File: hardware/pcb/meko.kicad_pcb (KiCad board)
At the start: 2 copper layers, 16 parts, among them IC1 MCP16502AD, IC2 MAYA-W386-00B, J1 Micro_SD_Card_Det1, J2 Micro_SD_Card_Det1, J4 Conn_ARM_JTAG_SWD_10, U1 SAMA7D65-4HB, U2 K4E8E324EB-EGCF, U3 MAX17260, U5 ECMF02-2AMX6, Y1 32kHz768, Y2 24MHz, Y3 32kHz768

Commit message: bunch of small audio changes
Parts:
- added IC3: TAC5212, Package_DFN_QFN:VQFN-24-1EP_4x4mm_P0.5mm_EP2.45x2.45mm, F.Cu at (100.9, 98.6)
- added J3: USB_C_Receptacle_USB2.0_16P, PCM_ckl-connector:USB_C_Receptacle_HRO_TYPE-C-31-M-12, F.Cu at (151.4, 55.9)
- added J5: 503480-1000, 503480-1000:5034801000, F.Cu at (95.8, 49.1)
- added J6: PJ-342, PCM_ckl-connector:Jack_3.5mm_SHOUHAN_PJ-342, F.Cu at (144.7, 39.9)
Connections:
- U1 pad P16: unconnected-(U1GPIO A&B-PA4-PadP16) -> /SAMA7/EXT.DAT1
- U1 pad R12: unconnected-(U1GPIO A&B-PA10-PadR12) -> /SAMA7/EXT.DAT3
- U1 pad T18: unconnected-(U1GPIO A&B-PA3-PadT18) -> /SAMA7/EXT.DAT0
- U1 pad U14: unconnected-(U1GPIO A&B-PA9-PadU14) -> /SAMA7/EXT.DAT2
- U1 pad U18: unconnected-(U1GPIO A&B-PA0-PadU18) -> /SAMA7/EXT.CK
- U1 pad V15: unconnected-(U1GPIO A&B-PA16-PadV15) -> /SAMA7/EXT.CD
- U1 pad V17: unconnected-(U1GPIO A&B-PA1-PadV17) -> /SAMA7/EXT.CMD

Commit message: bunch of small audio changes
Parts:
- added J7: PJ-342, PJ242:Jack_2.5mm_PJ242_6P_12x6.2x4mm_Horizontal, F.Cu at (148.6, 30.6)
- added U6: TPS7A2033PDBV, Package_TO_SOT_SMD:SOT-23-5, F.Cu at (152.0, 22.1)
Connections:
- IC3 pad 1: unconnected-(IC3-DREG-Pad1) -> Net-(IC3-DREG)
- IC3 pad 10: unconnected-(IC3-GPIO2-Pad10) -> /Audio/GPIO2
- IC3 pad 11: unconnected-(IC3-GPO1-Pad11) -> /Audio/GPO1
- IC3 pad 12: unconnected-(IC3-GPI1-Pad12) -> /Audio/GPI1
- IC3 pad 2: unconnected-(IC3-BCLK-Pad2) -> /Audio/BCLK
- IC3 pad 23: unconnected-(IC3-AVDD-Pad23) -> +3V3_AVDD
- IC3 pad 24: unconnected-(IC3-VREF-Pad24) -> Net-(IC3-VREF)
- IC3 pad 3: unconnected-(IC3-FSYNC-Pad3) -> /Audio/FSYNC
- IC3 pad 4: unconnected-(IC3-DOUT-Pad4) -> /Audio/DOUT
- IC3 pad 5: unconnected-(IC3-DIN-Pad5) -> /Audio/DIN
- IC3 pad 6: unconnected-(IC3-IOVDD-Pad6) -> +3V3
- IC3 pad 9: unconnected-(IC3-GPIO1-Pad9) -> /Audio/GPIO1
- J6 pad R1: (no net) -> unconnected-(J6-PadR1)
- J6 pad R1N: (no net) -> unconnected-(J6-PadR1N)
- J6 pad R2: (no net) -> unconnected-(J6-PadR2)
- J6 pad S: (no net) -> unconnected-(J6-PadS)
- J6 pad T: (no net) -> unconnected-(J6-PadT)
- J6 pad TN: (no net) -> unconnected-(J6-PadTN)

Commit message: moved stuff around
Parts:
- removed U2: K4E8E324EB-EGCF, K4E6E304EC-EGCG:FBGA-178_L11.5-W11.0_K4E6E304EC-TL
- added U7: DRV2605LDGS, Package_SO:TSSOP-10_3x3mm_P0.5mm, F.Cu at (157.5, 139.8)
- added U8: MT41K256M16TW, Package_BGA:Micron_FBGA-96_8x14mm_Layout9x16_P0.8mm, F.Cu at (105.3, 113.7)
- IC1: value MCP16502AD -> MCP16502AB
- J7: value PJ-342 -> PJ-242
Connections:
- net +1V2_DDR renamed +1V35_DDR
- IC1 pad 17: GND -> unconnected-(IC1-SELV2-Pad17)
- IC2 pad A2: unconnected-(IC2-1V8-PadA2) -> +1V8
- IC2 pad A3: unconnected-(IC2-SD_DAT[1]-PadA3) -> /Wireless/DAT1
- IC2 pad A4: unconnected-(IC2-SD_CLK-PadA4) -> /Wireless/CK
- IC2 pad A5: unconnected-(IC2-SD_DAT[3]-PadA5) -> /Wireless/DAT3
- IC2 pad A7: 3V3 -> +3V3
- IC2 pad B3: unconnected-(IC2-SD_DAT[0]-PadB3) -> /Wireless/DAT0
- IC2 pad B4: unconnected-(IC2-SD_CMD-PadB4) -> /Wireless/CMD
- IC2 pad B5: unconnected-(IC2-SD_DAT[2]-PadB5) -> /Wireless/DAT2
- IC2 pad B7: 3V3 -> +3V3
- IC2 pad D8: unconnected-(IC2-PCM_CLK-PadD8) -> /Wireless/BCLK
- IC2 pad E7: unconnected-(IC2-BT_HOST_WAKE-PadE7) -> /Wireless/BT.HOST_WAKE
- IC2 pad E8: unconnected-(IC2-PCM_MCLK-PadE8) -> /Wireless/MCLK
- IC2 pad E9: unconnected-(IC2-PCM_DIN-PadE9) -> /Wireless/DIN
- IC2 pad F7: unconnected-(IC2-WL_HOST_WAKE-PadF7) -> /Wireless/WL.HOST_WAKE
- IC2 pad F8: unconnected-(IC2-PCM_SYNC-PadF8) -> /Wireless/FSYNC
- IC2 pad F9: unconnected-(IC2-PCM_DOUT-PadF9) -> /Wireless/DOUT
- IC2 pad G8: unconnected-(IC2-UART_RX-PadG8) -> /Wireless/RX
- IC2 pad G9: unconnected-(IC2-UART_TX-PadG9) -> /Wireless/TX
- IC2 pad H7: unconnected-(IC2-JTAG_SEL-PadH7) -> GND
- IC2 pad H8: unconnected-(IC2-UART_CTSN-PadH8) -> /Wireless/CTSN
- IC2 pad H9: unconnected-(IC2-UART_RTSN-PadH9) -> /Wireless/RTSN
- IC2 pad J3: unconnected-(IC2-WL_EN-PadJ3) -> /Wireless/WL.EN
- IC2 pad J7: unconnected-(IC2-BT_EN-PadJ7) -> /Wireless/BT.EN
- IC2 pad J8: unconnected-(IC2-WL_DEV_WAKE-PadJ8) -> /Wireless/WL.DEV_WAKE
- IC2 pad J9: unconnected-(IC2-BT_DEV_WAKE-PadJ9) -> /Wireless/BT.DEV_WAKE
- IC2 pad K9: unconnected-(IC2-RF_ANT1-PadK9) -> Net-(IC2-ANT_EXT_FEED)
- IC2 pad L9: unconnected-(IC2-ANT_EXT_FEED-PadL9) -> Net-(IC2-ANT_EXT_FEED)
- IC3 pad 13: unconnected-(IC3-ADDR-Pad13) -> GND
- IC3 pad 14: unconnected-(IC3-MICBIAS-Pad14) -> +MICBIAS
- IC3 pad 15: unconnected-(IC3-IN1P-Pad15) -> /Audio/MIC
- IC3 pad 16: unconnected-(IC3-IN1M-Pad16) -> /Audio/LEFT-
- IC3 pad 19: unconnected-(IC3-OUT1M-Pad19) -> /Audio/LEFT-
- IC3 pad 20: unconnected-(IC3-OUT1P-Pad20) -> /Audio/LEFT+
- IC3 pad 21: unconnected-(IC3-OUT2P-Pad21) -> /Audio/RIGHT+
- IC3 pad 22: unconnected-(IC3-OUT2M-Pad22) -> /Audio/RIGHT-
- J6 pad R1: unconnected-(J6-PadR1) -> /Audio/RIGHT+
- J6 pad R2: unconnected-(J6-PadR2) -> /Audio/LEFT-
- J6 pad S: unconnected-(J6-PadS) -> /Audio/MIC
- J6 pad T: unconnected-(J6-PadT) -> /Audio/LEFT+
- J6 pad TN: unconnected-(J6-PadTN) -> /Audio/DET_3.5mm
- J7 pad R1: unconnected-(J7-PadR1) -> /Audio/RIGHT+
- J7 pad R2: unconnected-(J7-PadR2) -> /Audio/LEFT+
- J7 pad S: unconnected-(J7-PadS) -> /Audio/LEFT-
- J7 pad T: unconnected-(J7-PadT) -> /Audio/RIGHT-
- J7 pad TN: unconnected-(J7-PadTN) -> /Audio/DET_2.5mm
- U1 pad L9: unconnected-(U1DDR-DDR_A14-PadL9) -> /DDR/DDR_A14
- U1 pad M9: unconnected-(U1DDR-DDR_A11-PadM9) -> /DDR/DDR_A11
- U1 pad N10: unconnected-(U1DDR-DDR_WEN-PadN10) -> /DDR/~{WE}
- U1 pad P4: unconnected-(U1DDR-DDR_BA1-PadP4) -> /DDR/BA1
- U1 pad P5: unconnected-(U1DDR-DDR_A12-PadP5) -> /DDR/DDR_A12
- U1 pad R8: unconnected-(U1DDR-DDR_BA2-PadR8) -> /DDR/BA2
- U1 pad T3: unconnected-(U1DDR-DDR_A10-PadT3) -> /DDR/DDR_A10
- U1 pad T8: unconnected-(U1DDR-DDR_CASN-PadT8) -> /DDR/~{CAS}
- U1 pad U8: unconnected-(U1DDR-DDR_RASN-PadU8) -> /DDR/~{RAS}
- U1 pad V1: unconnected-(U1DDR-DDR_RESETN-PadV1) -> /DDR/~{RESET}
- U1 pad V2: unconnected-(U1DDR-DDR_A13-PadV2) -> /DDR/DDR_A13
- U1 pad V8: unconnected-(U1DDR-DDR_BA0-PadV8) -> /DDR/BA0

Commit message: looking over stuff, added caps
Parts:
- added C10: 4u7, Capacitor_SMD:C_0402_1005Metric, F.Cu at (113.3, 95.5)
- added C100: 4u7, Capacitor_SMD:C_0402_1005Metric, F.Cu at (81.3, 70.1)
- added C101: 100n, Capacitor_SMD:C_0402_1005Metric, F.Cu at (81.3, 72.1)
- added C102: 100n, Capacitor_SMD:C_0402_1005Metric, F.Cu at (81.3, 74.1)
- added C103: 100n, Capacitor_SMD:C_0402_1005Metric, F.Cu at (81.3, 76.1)
- added C104: 100n, Capacitor_SMD:C_0402_1005Metric, F.Cu at (81.3, 78.0)
- added C105: 100n, Capacitor_SMD:C_0402_1005Metric, F.Cu at (81.3, 80.0)
- added C106: 100n, Capacitor_SMD:C_0402_1005Metric, F.Cu at (81.3, 82.0)
- added C107: 100n, Capacitor_SMD:C_0402_1005Metric, F.Cu at (81.3, 83.9)
- added C108: 100n, Capacitor_SMD:C_0402_1005Metric, F.Cu at (84.2, 68.2)
- added C109: 100n, Capacitor_SMD:C_0402_1005Metric, F.Cu at (84.2, 70.1)
- added C11: 4u7, Capacitor_SMD:C_0402_1005Metric, F.Cu at (113.3, 97.5)
- added C110: 100n, Capacitor_SMD:C_0402_1005Metric, F.Cu at (84.2, 72.1)
- added C111: 100n, Capacitor_SMD:C_0402_1005Metric, F.Cu at (84.2, 74.1)
- added C112: 100n, Capacitor_SMD:C_0402_1005Metric, F.Cu at (84.2, 76.1)
- added C113: 100n, Capacitor_SMD:C_0402_1005Metric, F.Cu at (84.2, 78.0)
- added C114: 100n, Capacitor_SMD:C_0402_1005Metric, F.Cu at (84.2, 80.0)
- added C115: 4u7, Capacitor_SMD:C_0402_1005Metric, F.Cu at (84.2, 82.0)
- added C116: 100n, Capacitor_SMD:C_0402_1005Metric, F.Cu at (84.2, 83.9)
- added C117: 100n, Capacitor_SMD:C_0402_1005Metric, F.Cu at (87.1, 68.2)
- added C118: 100n, Capacitor_SMD:C_0402_1005Metric, F.Cu at (87.1, 70.1)
- added C119: 4u7, Capacitor_SMD:C_0402_1005Metric, F.Cu at (87.1, 72.1)
- added C12: 22u, Capacitor_SMD:C_0603_1608Metric, F.Cu at (107.0, 96.9)
- added C120: 100n, Capacitor_SMD:C_0402_1005Metric, F.Cu at (87.1, 74.1)
- added C121: 100n, Capacitor_SMD:C_0402_1005Metric, F.Cu at (87.1, 76.1)
- added C122: 100n, Capacitor_SMD:C_0402_1005Metric, F.Cu at (87.1, 78.0)
- added C123: 100n, Capacitor_SMD:C_0402_1005Metric, F.Cu at (87.1, 80.0)
- added C124: 100n, Capacitor_SMD:C_0402_1005Metric, F.Cu at (87.1, 82.0)
- added C125: 100n, Capacitor_SMD:C_0402_1005Metric, F.Cu at (87.1, 83.9)
- added C13: 4u7, Capacitor_SMD:C_0402_1005Metric, F.Cu at (116.1, 91.6)
- added C14: 22u, Capacitor_SMD:C_0603_1608Metric, F.Cu at (107.0, 99.4)
- added C15: 4u7, Capacitor_SMD:C_0402_1005Metric, F.Cu at (116.1, 93.6)
- added C16: 22u, Capacitor_SMD:C_0603_1608Metric, F.Cu at (107.0, 101.9)
- added C17: 4u7, Capacitor_SMD:C_0402_1005Metric, F.Cu at (116.1, 95.5)
- added C18: 4u7, Capacitor_SMD:C_0402_1005Metric, F.Cu at (116.1, 97.5)
- added C19: 4u7, Capacitor_SMD:C_0402_1005Metric, F.Cu at (119.0, 91.6)
- added C2: 1u, Capacitor_SMD:C_0402_1005Metric, F.Cu at (110.4, 91.6)
- added C20: 10u, Capacitor_SMD:C_0402_1005Metric, F.Cu at (119.0, 93.6)
- added C21: 1u, Capacitor_SMD:C_0402_1005Metric, F.Cu at (121.7, 125.4)
- added C22: 9p, Capacitor_SMD:C_0402_1005Metric, F.Cu at (69.9, 68.2)
- added C23: 9p, Capacitor_SMD:C_0402_1005Metric, F.Cu at (69.9, 70.1)
- added C24: 21pF, Capacitor_SMD:C_0402_1005Metric, F.Cu at (69.9, 72.1)
- added C25: 21pF, Capacitor_SMD:C_0402_1005Metric, F.Cu at (69.9, 74.1)
- added C26: 100n, Capacitor_SMD:C_0402_1005Metric, F.Cu at (133.2, 108.2)
- added C27: 9p, Capacitor_SMD:C_0402_1005Metric, F.Cu at (69.9, 76.1)
- added C28: 100n, Capacitor_SMD:C_0402_1005Metric, F.Cu at (80.9, 105.0)
- added C29: 100n, Capacitor_SMD:C_0402_1005Metric, F.Cu at (80.9, 106.9)
- added C3: 10u, Capacitor_SMD:C_0402_1005Metric, F.Cu at (110.4, 93.6)
- added C30: 9p, Capacitor_SMD:C_0402_1005Metric, F.Cu at (83.4, 130.7)
- added C31: 9p, Capacitor_SMD:C_0402_1005Metric, F.Cu at (83.4, 132.7)
- added C32: 1u, Capacitor_SMD:C_0402_1005Metric, F.Cu at (123.9, 98.3)
- added C33: 100n, Capacitor_SMD:C_0402_1005Metric, F.Cu at (123.9, 100.3)
- added C34: 10u, Capacitor_SMD:C_0402_1005Metric, F.Cu at (125.5, 86.6)
- added C35: 22u, Capacitor_SMD:C_0603_1608Metric, F.Cu at (126.1, 81.9)
- added C36: 22u, Capacitor_SMD:C_0603_1608Metric, F.Cu at (126.1, 84.4)
- added C37: 1u, Capacitor_SMD:C_0402_1005Metric, F.Cu at (123.9, 102.3)
- added C39: 1u, Capacitor_SMD:C_0402_1005Metric, F.Cu at (83.4, 134.7)
- added C4: 47n, Capacitor_SMD:C_0402_1005Metric, F.Cu at (110.4, 95.5)
- added C41: 1u, Capacitor_SMD:C_0402_1005Metric, F.Cu at (110.2, 125.4)
- added C42: 1u, Capacitor_SMD:C_0402_1005Metric, F.Cu at (83.4, 136.6)
- added C43: 1u, Capacitor_SMD:C_0402_1005Metric, F.Cu at (119.0, 95.5)
- added C44: 1u, Capacitor_SMD:C_0402_1005Metric, F.Cu at (119.0, 97.5)
- added C45: 10u, Capacitor_SMD:C_0402_1005Metric, F.Cu at (110.2, 127.3)
- added C46: 10u, Capacitor_SMD:C_0402_1005Metric, F.Cu at (110.2, 129.3)
- added C47: 1u, Capacitor_SMD:C_0402_1005Metric, F.Cu at (110.2, 131.3)
- added C48: 4u7, Capacitor_SMD:C_0402_1005Metric, F.Cu at (80.9, 108.9)
- added C49: 100n, Capacitor_SMD:C_0402_1005Metric, F.Cu at (80.9, 110.9)
- added C5: 22u, Capacitor_SMD:C_0603_1608Metric, F.Cu at (107.0, 91.9)
- added C50: 100n, Capacitor_SMD:C_0402_1005Metric, F.Cu at (80.9, 112.8)
- added C51: 100n, Capacitor_SMD:C_0402_1005Metric, F.Cu at (80.9, 114.8)
- added C52: 100n, Capacitor_SMD:C_0402_1005Metric, F.Cu at (83.8, 105.0)
- added C53: 100n, Capacitor_SMD:C_0402_1005Metric, F.Cu at (83.8, 106.9)
- added C54: 100n, Capacitor_SMD:C_0402_1005Metric, F.Cu at (83.8, 108.9)
- added C55: 100n, Capacitor_SMD:C_0402_1005Metric, F.Cu at (83.8, 110.9)
- added C56: 100n, Capacitor_SMD:C_0402_1005Metric, F.Cu at (83.8, 112.8)
- added C57: 100n, Capacitor_SMD:C_0402_1005Metric, F.Cu at (83.8, 114.8)
- added C58: 100n, Capacitor_SMD:C_0402_1005Metric, F.Cu at (86.6, 105.0)
- added C59: 100n, Capacitor_SMD:C_0402_1005Metric, F.Cu at (86.6, 106.9)
- added C6: 4u7, Capacitor_SMD:C_0402_1005Metric, F.Cu at (110.4, 97.5)
- added C60: 100n, Capacitor_SMD:C_0402_1005Metric, F.Cu at (86.6, 108.9)
- added C61: 100n, Capacitor_SMD:C_0402_1005Metric, F.Cu at (86.6, 110.9)
- added C62: 100n, Capacitor_SMD:C_0402_1005Metric, F.Cu at (86.6, 112.8)
- added C63: 100n, Capacitor_SMD:C_0402_1005Metric, F.Cu at (86.6, 114.8)
- added C64: 100n, Capacitor_SMD:C_0402_1005Metric, F.Cu at (89.5, 105.0)
- added C65: 100n, Capacitor_SMD:C_0402_1005Metric, F.Cu at (89.5, 106.9)
- added C66: 100n, Capacitor_SMD:C_0402_1005Metric, F.Cu at (89.5, 108.9)
- added C67: 4u7, Capacitor_SMD:C_0402_1005Metric, F.Cu at (89.5, 110.9)
- added C68: 4u7, Capacitor_SMD:C_0402_1005Metric, F.Cu at (69.9, 78.0)
- added C69: 100n, Capacitor_SMD:C_0402_1005Metric, F.Cu at (69.9, 80.0)
- added C7: 470n, Capacitor_SMD:C_0402_1005Metric, F.Cu at (113.3, 91.6)
- added C70: 100n, Capacitor_SMD:C_0402_1005Metric, F.Cu at (69.9, 82.0)
- added C71: 100n, Capacitor_SMD:C_0402_1005Metric, F.Cu at (69.9, 83.9)
- added C72: 100n, Capacitor_SMD:C_0402_1005Metric, F.Cu at (72.7, 68.2)
- added C73: 100n, Capacitor_SMD:C_0402_1005Metric, F.Cu at (72.7, 70.1)
- added C74: 100n, Capacitor_SMD:C_0402_1005Metric, F.Cu at (72.7, 72.1)
- added C75: 100n, Capacitor_SMD:C_0402_1005Metric, F.Cu at (72.7, 74.1)
- added C76: 100n, Capacitor_SMD:C_0402_1005Metric, F.Cu at (72.7, 76.1)
- added C77: 100n, Capacitor_SMD:C_0402_1005Metric, F.Cu at (72.7, 78.0)
- added C78: 100n, Capacitor_SMD:C_0402_1005Metric, F.Cu at (72.7, 80.0)
- added C79: 100n, Capacitor_SMD:C_0402_1005Metric, F.Cu at (72.7, 82.0)
- added C8: 100n, Capacitor_SMD:C_0402_1005Metric, F.Cu at (113.3, 93.6)
- added C80: 100n, Capacitor_SMD:C_0402_1005Metric, F.Cu at (72.7, 83.9)
- added C81: 100n, Capacitor_SMD:C_0402_1005Metric, F.Cu at (75.6, 68.2)
- added C82: 100n, Capacitor_SMD:C_0402_1005Metric, F.Cu at (75.6, 70.1)
- added C83: 4u7, Capacitor_SMD:C_0402_1005Metric, F.Cu at (75.6, 72.1)
- added C84: 100n, Capacitor_SMD:C_0402_1005Metric, F.Cu at (75.6, 74.1)
- added C85: 100n, Capacitor_SMD:C_0402_1005Metric, F.Cu at (75.6, 76.1)
- added C86: 100n, Capacitor_SMD:C_0402_1005Metric, F.Cu at (75.6, 78.0)
- added C87: 100n, Capacitor_SMD:C_0402_1005Metric, F.Cu at (75.6, 80.0)
- added C88: 100n, Capacitor_SMD:C_0402_1005Metric, F.Cu at (75.6, 82.0)
- added C89: 4u7, Capacitor_SMD:C_0402_1005Metric, F.Cu at (75.6, 83.9)
- added C9: 22u, Capacitor_SMD:C_0603_1608Metric, F.Cu at (107.0, 94.4)
- added C90: 4u7, Capacitor_SMD:C_0402_1005Metric, F.Cu at (78.5, 68.2)
- added C91: 100n, Capacitor_SMD:C_0402_1005Metric, F.Cu at (78.5, 70.1)
- added C92: 100n, Capacitor_SMD:C_0402_1005Metric, F.Cu at (78.5, 72.1)
- added C93: 100n, Capacitor_SMD:C_0402_1005Metric, F.Cu at (78.5, 74.1)
- added C94: 100n, Capacitor_SMD:C_0402_1005Metric, F.Cu at (78.5, 76.1)
- added C95: 100n, Capacitor_SMD:C_0402_1005Metric, F.Cu at (78.5, 78.0)
- added C96: 100n, Capacitor_SMD:C_0402_1005Metric, F.Cu at (78.5, 80.0)
- added C97: 100n, Capacitor_SMD:C_0402_1005Metric, F.Cu at (78.5, 82.0)
- added C98: 100n, Capacitor_SMD:C_0402_1005Metric, F.Cu at (78.5, 83.9)
- added C99: 100n, Capacitor_SMD:C_0402_1005Metric, F.Cu at (81.3, 68.2)
- added L1: 2u2, Inductor_SMD:L_1008_2520Metric, F.Cu at (99.6, 92.5)
- added L2: 2u2, Inductor_SMD:L_1008_2520Metric, F.Cu at (99.6, 96.2)
- added L3: 2u2, Inductor_SMD:L_1008_2520Metric, F.Cu at (99.6, 100.0)
- added L4: 2u2, Inductor_SMD:L_1008_2520Metric, F.Cu at (99.6, 103.7)
- added L5: 2u2, Inductor_SMD:L_1008_2520Metric, F.Cu at (99.6, 107.5)
- added R1: 240R, Resistor_SMD:R_0402_1005Metric, F.Cu at (80.9, 116.8)
- added R10: 4k02, Resistor_SMD:R_0402_1005Metric, F.Cu at (90.0, 72.2)
- added R11: 1k, Resistor_SMD:R_0402_1005Metric, F.Cu at (80.9, 118.8)
- added R12: 1k, Resistor_SMD:R_0402_1005Metric, F.Cu at (80.9, 120.8)
- added R13: 47k, Resistor_SMD:R_0402_1005Metric, F.Cu at (116.8, 81.6)
- added R14: 47k, Resistor_SMD:R_0402_1005Metric, F.Cu at (116.8, 83.6)
- added R15: 47k, Resistor_SMD:R_0402_1005Metric, F.Cu at (116.8, 85.6)
- added R16: 47k, Resistor_SMD:R_0402_1005Metric, F.Cu at (116.8, 87.6)
- added R17: 47k, Resistor_SMD:R_0402_1005Metric, F.Cu at (119.7, 81.6)
- added R18: 10k, Resistor_SMD:R_0402_1005Metric, F.Cu at (119.7, 83.6)
- added R19: 47k, Resistor_SMD:R_0402_1005Metric, F.Cu at (119.7, 85.6)
- added R2: 240R, Resistor_SMD:R_0402_1005Metric, F.Cu at (90.0, 68.2)
- added R20: 47k, Resistor_SMD:R_0402_1005Metric, F.Cu at (119.7, 87.6)
- added R21: 47k, Resistor_SMD:R_0402_1005Metric, F.Cu at (122.6, 81.6)
- added R22: 47k, Resistor_SMD:R_0402_1005Metric, F.Cu at (122.6, 83.6)
- added R23: 47k, Resistor_SMD:R_0402_1005Metric, F.Cu at (122.6, 85.6)
- added R24: 10k, Resistor_SMD:R_0402_1005Metric, F.Cu at (122.6, 87.6)
- added R25: 10k, Resistor_SMD:R_0402_1005Metric, F.Cu at (90.0, 74.2)
- added R26: 100k, Resistor_SMD:R_0402_1005Metric, F.Cu at (114.4, 114.9)
- added R27: 100k, Resistor_SMD:R_0402_1005Metric, F.Cu at (114.4, 116.9)
- added R28: 1k, Resistor_SMD:R_0402_1005Metric, F.Cu at (114.4, 118.9)
- added R29: 47k, Resistor_SMD:R_0402_1005Metric, F.Cu at (83.4, 124.8)
- added R3: 100R, Resistor_SMD:R_0402_1005Metric, F.Cu at (103.5, 91.6)
- added R30: 47k, Resistor_SMD:R_0402_1005Metric, F.Cu at (83.4, 126.7)
- added R31: 47k, Resistor_SMD:R_0402_1005Metric, F.Cu at (83.4, 128.7)
- added R32: 47k, Resistor_SMD:R_0402_1005Metric, F.Cu at (86.3, 124.8)
- added R33: 47k, Resistor_SMD:R_0402_1005Metric, F.Cu at (86.3, 126.7)
- added R34: 10k, Resistor_SMD:R_0402_1005Metric, F.Cu at (86.3, 128.7)
- added R35: 10k, Resistor_SMD:R_0402_1005Metric, F.Cu at (89.2, 124.8)
- added R36: 10k, Resistor_SMD:R_0402_1005Metric, F.Cu at (90.0, 76.1)
- added R37: 10k, Resistor_SMD:R_0402_1005Metric, F.Cu at (90.0, 78.1)
- added R38: 10k, Resistor_SMD:R_0402_1005Metric, F.Cu at (89.2, 126.7)
- added R39: 10k, Resistor_SMD:R_0402_1005Metric, F.Cu at (89.2, 128.7)
- added R4: 10m, Resistor_SMD:R_0402_1005Metric, F.Cu at (103.5, 93.6)
- added R40: 10k, Resistor_SMD:R_0402_1005Metric, F.Cu at (92.9, 68.2)
- added R41: 10k, Resistor_SMD:R_0402_1005Metric, F.Cu at (133.2, 106.3)
- added R42: 10k, Resistor_SMD:R_0402_1005Metric, F.Cu at (126.8, 98.3)
- added R43: 10k, Resistor_SMD:R_0402_1005Metric, F.Cu at (103.5, 103.5)
- added R44: 10k, Resistor_SMD:R_0402_1005Metric, F.Cu at (103.5, 105.5)
- added R45: 16k9, Resistor_SMD:R_0402_1005Metric, F.Cu at (92.9, 70.2)
- added R46: 16k9, Resistor_SMD:R_0402_1005Metric, F.Cu at (92.9, 72.2)
- added R47: 16k9, Resistor_SMD:R_0402_1005Metric, F.Cu at (92.9, 74.2)
- added R48: 16k9, Resistor_SMD:R_0402_1005Metric, F.Cu at (92.9, 76.1)
- added R5: 1k5, Resistor_SMD:R_0402_1005Metric, F.Cu at (103.5, 95.6)
- added R6: 10k, Resistor_SMD:R_0402_1005Metric, F.Cu at (103.5, 97.6)
- added R7: 10k, Resistor_SMD:R_0402_1005Metric, F.Cu at (103.5, 99.6)
- added R8: 10k, Resistor_SMD:R_0402_1005Metric, F.Cu at (103.5, 101.5)
- added R9: 5k62, Resistor_SMD:R_0402_1005Metric, F.Cu at (90.0, 70.2)
- moved J7 107.9 mm to (103.1, 128.4), turned to 0 degrees
- moved U6 92.8 mm to (117.2, 108.2), turned to 0 degrees
- moved IC2 87.6 mm to (75.2, 132.5)
- moved J6 86.8 mm to (109.4, 119.1), turned to 0 degrees
- moved J3 68.7 mm to (126.1, 119.7)
- moved J5 54.8 mm to (127.3, 94.0), turned to 0 degrees
- moved U7 45.0 mm to (126.1, 107.6)
- moved U3 44.5 mm to (112.0, 108.1)
- moved D5 42.4 mm to (99.1, 110.6)
- moved Y3 42.2 mm to (87.4, 131.5)
- moved U1 39.8 mm to (76.9, 93.4)
- moved Y2 38.1 mm to (88.1, 95.6)
- moved IC3 32.3 mm to (115.1, 127.5)
- moved U8 31.4 mm to (73.9, 112.5)
- moved U5 28.6 mm to (133.8, 125.8)
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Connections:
- net /USB/CC1 renamed /Power/CC1
- net /USB/CC2 renamed /Power/CC2
- IC1 pad 24: Net-(IC1-NSTRT) -> /Buttons/PWR
- IC1 pad 5: /Power/SDA -> /Audio/SDA
- IC1 pad 6: /Power/SCL -> /Audio/SCL
- IC2 pad A3: /Wireless/DAT1 -> /SAMA7/WIFI.DAT1
- IC2 pad A4: /Wireless/CK -> /SAMA7/WIFI.CK
- IC2 pad A5: /Wireless/DAT3 -> /SAMA7/WIFI.DAT3
- IC2 pad B3: /Wireless/DAT0 -> /SAMA7/WIFI.DAT0
- IC2 pad B4: /Wireless/CMD -> /SAMA7/WIFI.CMD
- IC2 pad B5: /Wireless/DAT2 -> /SAMA7/WIFI.DAT2
- IC2 pad D8: /Wireless/BCLK -> /SAMA7/BT.BCLK
- IC2 pad E7: /Wireless/BT.HOST_WAKE -> /SAMA7/BT.HOST_WAKE
- IC2 pad E8: /Wireless/MCLK -> /SAMA7/BT.MCLK
- IC2 pad E9: /Wireless/DIN -> /SAMA7/BT.DIN
- IC2 pad F7: /Wireless/WL.HOST_WAKE -> /SAMA7/WL.HOST_WAKE
- IC2 pad F8: /Wireless/FSYNC -> /SAMA7/BT.FSYNC
- IC2 pad F9: /Wireless/DOUT -> /SAMA7/BT.DOUT
- IC2 pad G8: /Wireless/RX -> /SAMA7/BT.RX
- IC2 pad G9: /Wireless/TX -> /SAMA7/BT.TX
- IC2 pad H8: /Wireless/CTSN -> /SAMA7/BT.CTSN
- IC2 pad H9: /Wireless/RTSN -> /SAMA7/BT.RTSN
- IC2 pad J3: /Wireless/WL.EN -> /SAMA7/WL.EN
- IC2 pad J7: /Wireless/BT.EN -> /SAMA7/BT.EN
- IC2 pad J8: /Wireless/WL.DEV_WAKE -> /SAMA7/WL.DEV_WAKE
- IC2 pad J9: /Wireless/BT.DEV_WAKE -> /SAMA7/BT.DEV_WAKE
- IC3 pad 8: /Audio/SCL -> /Audio/SDA
- J1 pad 1: /SD Cards/EXT.DAT2 -> /SAMA7/EXT.DAT2
- J1 pad 2: /SD Cards/EXT.DAT3 -> /SAMA7/EXT.DAT3
- J1 pad 3: /SD Cards/EXT.CMD -> /SAMA7/EXT.CMD
- J1 pad 5: /SD Cards/EXT.CK -> /SAMA7/EXT.CK
- J1 pad 7: /SD Cards/EXT.DAT0 -> /SAMA7/EXT.DAT0
- J1 pad 8: /SD Cards/EXT.DAT1 -> /SAMA7/EXT.DAT1
- J1 pad 9: /SD Cards/EXT.CD -> /SAMA7/EXT.CD
- J2 pad 1: /SD Cards/BOOT.DAT2 -> /SAMA7/BOOT.DAT2
- J2 pad 2: /SD Cards/BOOT.DAT3 -> /SAMA7/BOOT.DAT3
- J2 pad 3: /SD Cards/BOOT.CMD -> /SAMA7/BOOT.CMD
- J2 pad 5: /SD Cards/BOOT.CK -> /SAMA7/BOOT.CK
- J2 pad 7: /SD Cards/BOOT.DAT0 -> /SAMA7/BOOT.DAT0
- J2 pad 8: /SD Cards/BOOT.DAT1 -> /SAMA7/BOOT.DAT1
- J2 pad 9: /SD Cards/BOOT.CD -> /SAMA7/BOOT.CD
- J4 pad 10: /SAMA7/~{RST} -> /Power/~{RST}
- J6 pad TN: /Audio/DET_3.5mm -> /Audio/~{DET}_3.5mm
- J7 pad TN: /Audio/DET_2.5mm -> /Audio/~{DET}_2.5mm
- U1 pad A16: unconnected-(U1GPIO C&D&E-PC31-PadA16) -> /SAMA7/WIFI.DAT2
- U1 pad A18: unconnected-(U1GPIO C&D&E-PD1-PadA18) -> /SAMA7/WL.HOST_WAKE
- U1 pad A6: /SAMA7/LPM -> /Power/LPM
- U1 pad A8: /SAMA7/~{WKUP} -> /Power/~{WKUP}
- U1 pad AA16: unconnected-(U1GPIO C&D&E-PE8-PadAA16) -> /SAMA7/TOUCH_~{RST}
- U1 pad AA19: unconnected-(U1GPIO C&D&E-PE10-PadAA19) -> /SAMA7/HAPT_~{INT}
- U1 pad AA20: unconnected-(U1GPIO A&B-PA23-PadAA20) -> /Display/SCS
- U1 pad B1: unconnected-(U1GPIO C&D&E-PC7-PadB1) -> /Audio/SDA
- U1 pad B13: unconnected-(U1PERIs-SDMMC1_CAL-PadB13) -> Net-(U1PERIs-SDMMC1_CAL)
- U1 pad B16: unconnected-(U1GPIO C&D&E-PC29-PadB16) -> /SAMA7/WIFI.DAT0
- U1 pad B19: unconnected-(U1GPIO C&D&E-PD30-PadB19) -> /Power/CHG_~{INT}
- U1 pad B21: unconnected-(U1GPIO A&B-PA25-PadB21) -> /Display/DISP
- U1 pad B4: /SAMA7/PWRHLD -> /Power/PWRHLD
- U1 pad C1: unconnected-(U1GPIO C&D&E-PC11-PadC1) -> /Power/HPM
- U1 pad C15: unconnected-(U1GPIO C&D&E-PC27-PadC15) -> /SAMA7/WIFI.CMD
- U1 pad C16: unconnected-(U1GPIO C&D&E-PD0-PadC16) -> /SAMA7/WIFI.DAT3
- U1 pad C17: unconnected-(U1PWR-VDDIOP1-PadC17) -> +1V8
- U1 pad C2: unconnected-(U1GPIO C&D&E-PC4-PadC2) -> /Audio/~{DET}_2.5mm
- U1 pad D16: unconnected-(U1GPIO C&D&E-PC28-PadD16) -> /SAMA7/WIFI.CK
- U1 pad D17: unconnected-(U1GPIO C&D&E-PC30-PadD17) -> /SAMA7/WIFI.DAT1
- U1 pad D2: unconnected-(U1PWR-ADVREFP-PadD2) -> +2V5
- U1 pad D20: unconnected-(U1GPIO C&D&E-PE3-PadD20) -> /SAMA7/TOUCH.SDA
- U1 pad D3: /SAMA7/~{RST} -> /Power/~{RST}
- U1 pad D4: unconnected-(U1GPIO C&D&E-PC17-PadD4) -> /Audio/DIN
- U1 pad E14: unconnected-(U1PERIs-SDMMC2_CAL-PadE14) -> Net-(U1PERIs-SDMMC2_CAL)
- U1 pad E3: unconnected-(U1PWR-VDDOUT25-PadE3) -> +2V5
- U1 pad E5: Net-(U1PWR-VDDANA-PadE5) -> +2V5
- U1 pad E8: Net-(JP3-C) -> /SAMA7/VBAT
- U1 pad F13: unconnected-(U1PWR-VDDSDMMC2-PadF13) -> +1V8
- U1 pad F14: unconnected-(U1GPIO C&D&E-PD9-PadF14) -> /Buttons/VOL-
- U1 pad F18: /SAMA7/UART_SAMBA_RX -> /SAMA7/UART_SAMBA_TX
- U1 pad F19: unconnected-(U1GPIO C&D&E-PD22-PadF19) -> /Audio/GPIO1
- U1 pad F20: unconnected-(U1GPIO C&D&E-PD31-PadF20) -> /Power/FUEL_~{INT}
- U1 pad F3: unconnected-(U1GPIO C&D&E-PC15-PadF3) -> /Audio/FSYNC
- U1 pad F9: unconnected-(U1PWR-VDDSDMMC1-PadF9) -> +3V3
- U1 pad G13: unconnected-(U1GPIO C&D&E-PD2-PadG13) -> /SAMA7/WL.DEV_WAKE
- U1 pad G14: unconnected-(U1GPIO C&D&E-PD8-PadG14) -> /Buttons/VOL+
- U1 pad G16: unconnected-(U1GPIO C&D&E-PD10-PadG16) -> /Buttons/SIDE_L
- U1 pad G18: unconnected-(U1GPIO C&D&E-PD23-PadG18) -> /Audio/GPIO2
- U1 pad G19: unconnected-(U1GPIO C&D&E-PD24-PadG19) -> /Audio/GPO1
- U1 pad G8: unconnected-(U1GPIO C&D&E-PC3-PadG8) -> /Audio/~{DET}_3.5mm
- U1 pad H11: unconnected-(U1GPIO C&D&E-PD11-PadH11) -> /Buttons/SIDE_R
- U1 pad H16: /SAMA7/UART_SAMBA_TX -> /SAMA7/UART_SAMBA_RX
- U1 pad H19: unconnected-(U1PWR-VDDGMAC1-PadH19) -> +3V3
- U1 pad H4: unconnected-(U1GPIO C&D&E-PC16-PadH4) -> /Audio/BCLK
- U1 pad H5: unconnected-(U1GPIO C&D&E-PC12-PadH5) -> /Power/~{INT}
- U1 pad H6: unconnected-(U1GPIO C&D&E-PC6-PadH6) -> /Audio/SCL
- U1 pad J6: Net-(U1PWR-VDDANA-PadE5) -> +2V5
- U1 pad J7: unconnected-(U1GPIO C&D&E-PC14-PadJ7) -> /Audio/DOUT
- U1 pad K12: unconnected-(U1GPIO C&D&E-PE2-PadK12) -> /SAMA7/TOUCH.SCL
- U1 pad K8: unconnected-(U1PERIs-AUDIOCLK-PadK8) -> Net-(U1PERIs-AUDIOCLK)
- U1 pad K9: unconnected-(U1GPIO C&D&E-PD25-PadK9) -> /Audio/GPI1
- U1 pad L14: unconnected-(U1GPIO A&B-PB19-PadL14) -> /SAMA7/BT.HOST_WAKE
- U1 pad L19: unconnected-(U1PWR-VDDGMAC0-PadL19) -> +3V3
- U1 pad M12: unconnected-(U1GPIO A&B-PB20-PadM12) -> /SAMA7/BT.DEV_WAKE
- U1 pad M13: unconnected-(U1PERIs-QSPI0_CAL-PadM13) -> Net-(U1PERIs-QSPI0_CAL)
- U1 pad M14: unconnected-(U1GPIO A&B-PB17-PadM14) -> /SAMA7/BT.DIN
- U1 pad M15: unconnected-(U1GPIO A&B-PB15-PadM15) -> /SAMA7/BT.FSYNC
- U1 pad N14: unconnected-(U1GPIO A&B-PB13-PadN14) -> /SAMA7/WL.EN
- U1 pad N15: unconnected-(U1GPIO A&B-PB14-PadN15) -> /SAMA7/BT.BCLK
- U1 pad N20: unconnected-(U1GPIO A&B-PB16-PadN20) -> /SAMA7/BT.DOUT
- U1 pad N21: unconnected-(U1GPIO A&B-PB18-PadN21) -> /SAMA7/BT.MCLK
- U1 pad P10: unconnected-(U1GPIO A&B-PA22-PadP10) -> /Display/SCLK
- U1 pad P17: unconnected-(U1GPIO A&B-PB10-PadP17) -> /SAMA7/BT.CTSN
- U1 pad P18: unconnected-(U1GPIO A&B-PB12-PadP18) -> /SAMA7/BT.RTSN
- U1 pad P19: unconnected-(U1PWR-VDDQSPI0-PadP19) -> +1V8
- U1 pad P9: unconnected-(U1GPIO A&B-PA24-PadP9) -> /Display/SI
- U1 pad R16: unconnected-(U1PERIs-SDMMC0_CAL-PadR16) -> Net-(U1PERIs-SDMMC0_CAL)
- U1 pad R18: unconnected-(U1GPIO A&B-PB9-PadR18) -> /SAMA7/BT.RX
- U1 pad R19: unconnected-(U1GPIO A&B-PB11-PadR19) -> /SAMA7/BT.EN
- U1 pad T13: unconnected-(U1PWR-VDDIOP0-PadT13) -> +3V3
- U1 pad T16: unconnected-(U1PWR-VDDDPHY-PadT16) -> +2V5
- U1 pad T19: unconnected-(U1GPIO A&B-PB8-PadT19) -> /SAMA7/BT.TX
- U1 pad W11: unconnected-(U1PWR-VDDLVDS-PadW11) -> +3V3
- U1 pad W14: unconnected-(U1PWR-VDDIN25-PadW14) -> +2V5
- U1 pad W17: unconnected-(U1PWR-VDDSDMMC0-PadW17) -> +3V3
- U1 pad Y15: unconnected-(U1GPIO C&D&E-PE7-PadY15) -> /SAMA7/TOUCH_~{INT}
- U1 pad Y19: unconnected-(U1GPIO C&D&E-PE11-PadY19) -> /SAMA7/HAPT_EN
- U3 pad 13: /Power/SCL -> /Audio/SCL
- U3 pad 14: /Power/SDA -> /Audio/SDA
- U5 pad 5: /USB/D- -> /SAMA7/D-
- U5 pad 6: /USB/D+ -> /SAMA7/D+
- U7 pad 2: unconnected-(U7-SCL-Pad2) -> /Touch Pad/SCL
- U7 pad 3: unconnected-(U7-SDA-Pad3) -> /Touch Pad/SDA
- U7 pad 4: unconnected-(U7-IN/TRIG-Pad4) -> /SAMA7/HAPT_~{INT}
- U7 pad 5: unconnected-(U7-EN-Pad5) -> /SAMA7/HAPT_EN

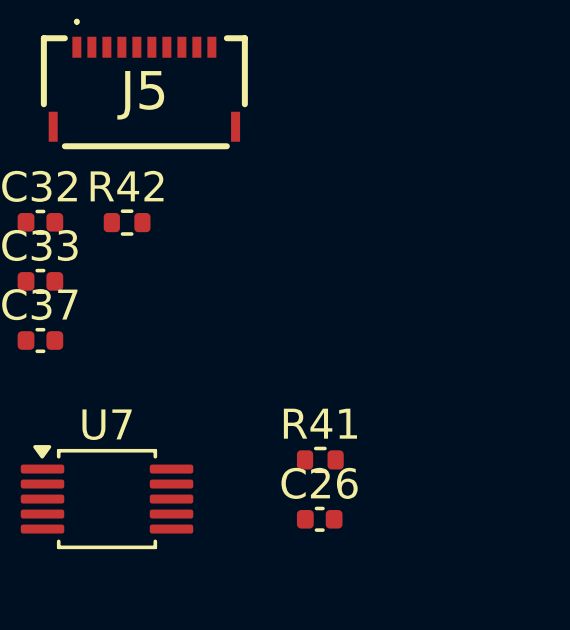
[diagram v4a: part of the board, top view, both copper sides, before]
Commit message: added bq25640 footprint
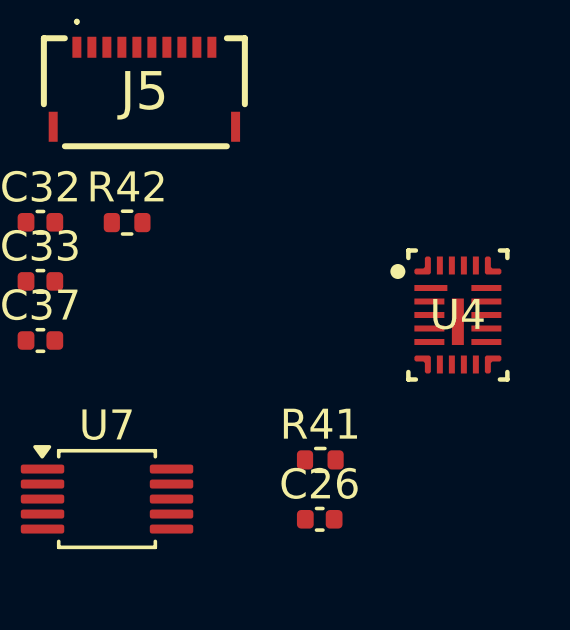
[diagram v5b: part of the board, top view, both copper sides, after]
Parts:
- added U4: BQ25640, BQ25640:VDL0023A-MFG, F.Cu at (137.8, 101.4)

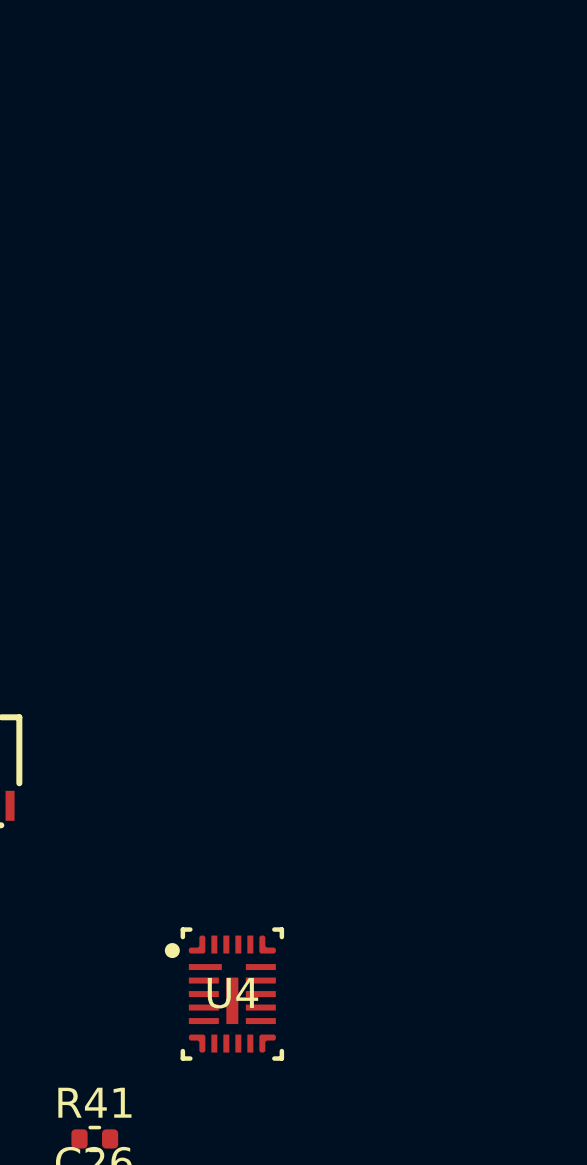
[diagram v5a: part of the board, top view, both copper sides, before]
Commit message: added buttons
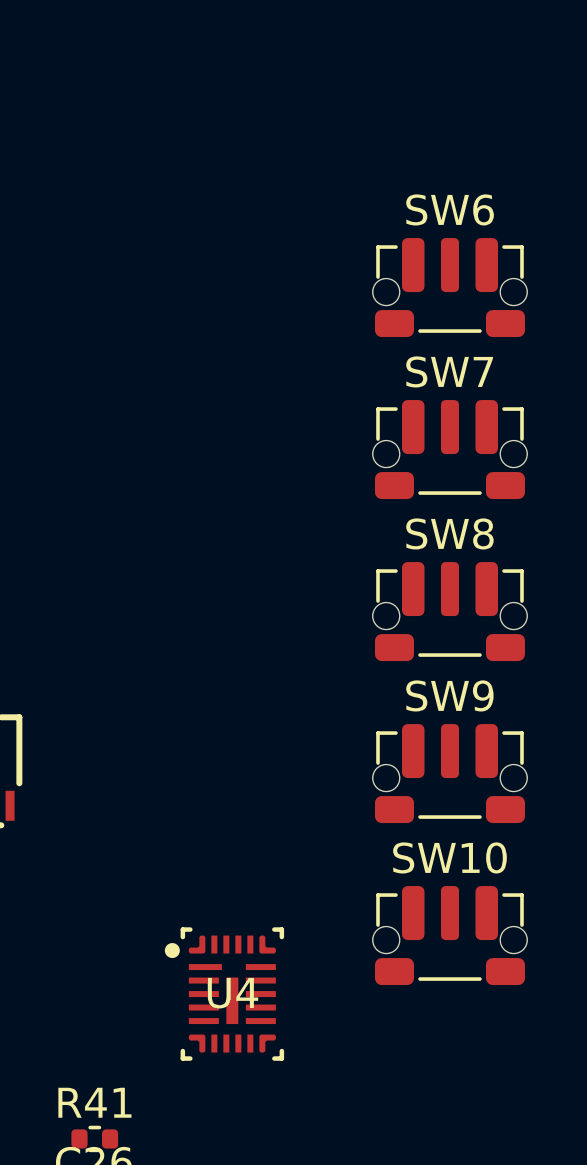
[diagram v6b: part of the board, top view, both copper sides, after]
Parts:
- added SW10: SW_Push, Button_Switch_SMD:SW_Push_1P1T-MP_NO_Horizontal_Alps_SKRTLAE010, F.Cu at (145.1, 99.6)
- added SW6: SW_Push, Button_Switch_SMD:SW_Push_1P1T-MP_NO_Horizontal_Alps_SKRTLAE010, F.Cu at (145.1, 78.0)
- added SW7: SW_Push, Button_Switch_SMD:SW_Push_1P1T-MP_NO_Horizontal_Alps_SKRTLAE010, F.Cu at (145.1, 83.4)
- added SW8: SW_Push, Button_Switch_SMD:SW_Push_1P1T-MP_NO_Horizontal_Alps_SKRTLAE010, F.Cu at (145.1, 88.8)
- added SW9: SW_Push, Button_Switch_SMD:SW_Push_1P1T-MP_NO_Horizontal_Alps_SKRTLAE010, F.Cu at (145.1, 94.2)
